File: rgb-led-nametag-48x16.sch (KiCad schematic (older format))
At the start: 21 parts, among them J1 USB_C_Receptacle_USB2.0, J2 TagConnect_TC2030_SWD, U25 STM32F722RETx, U26 SRV05-4, U27 TPS63001

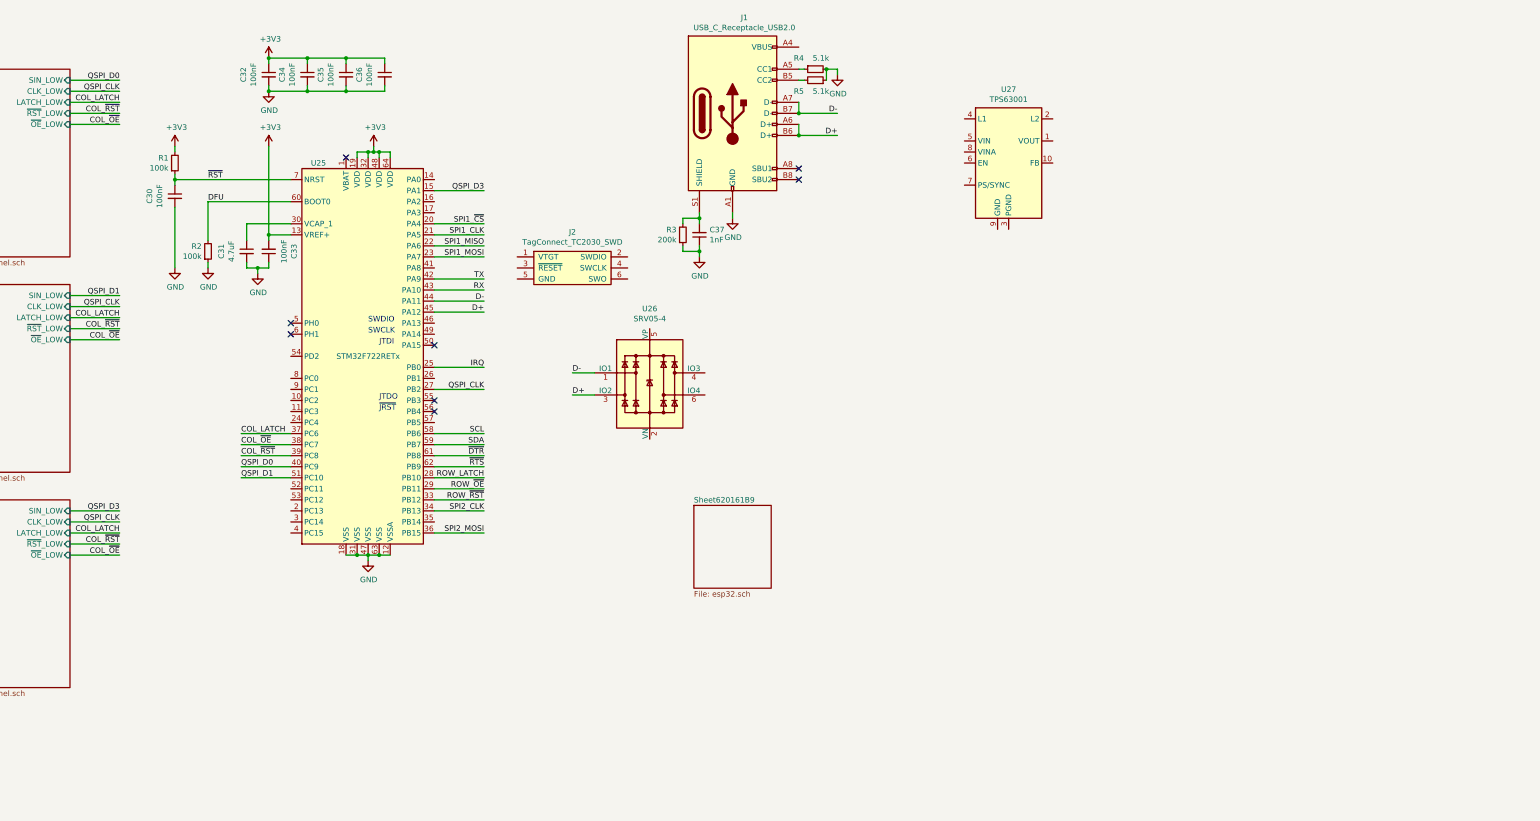
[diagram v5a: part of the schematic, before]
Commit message: Route ESP32 SPI bus
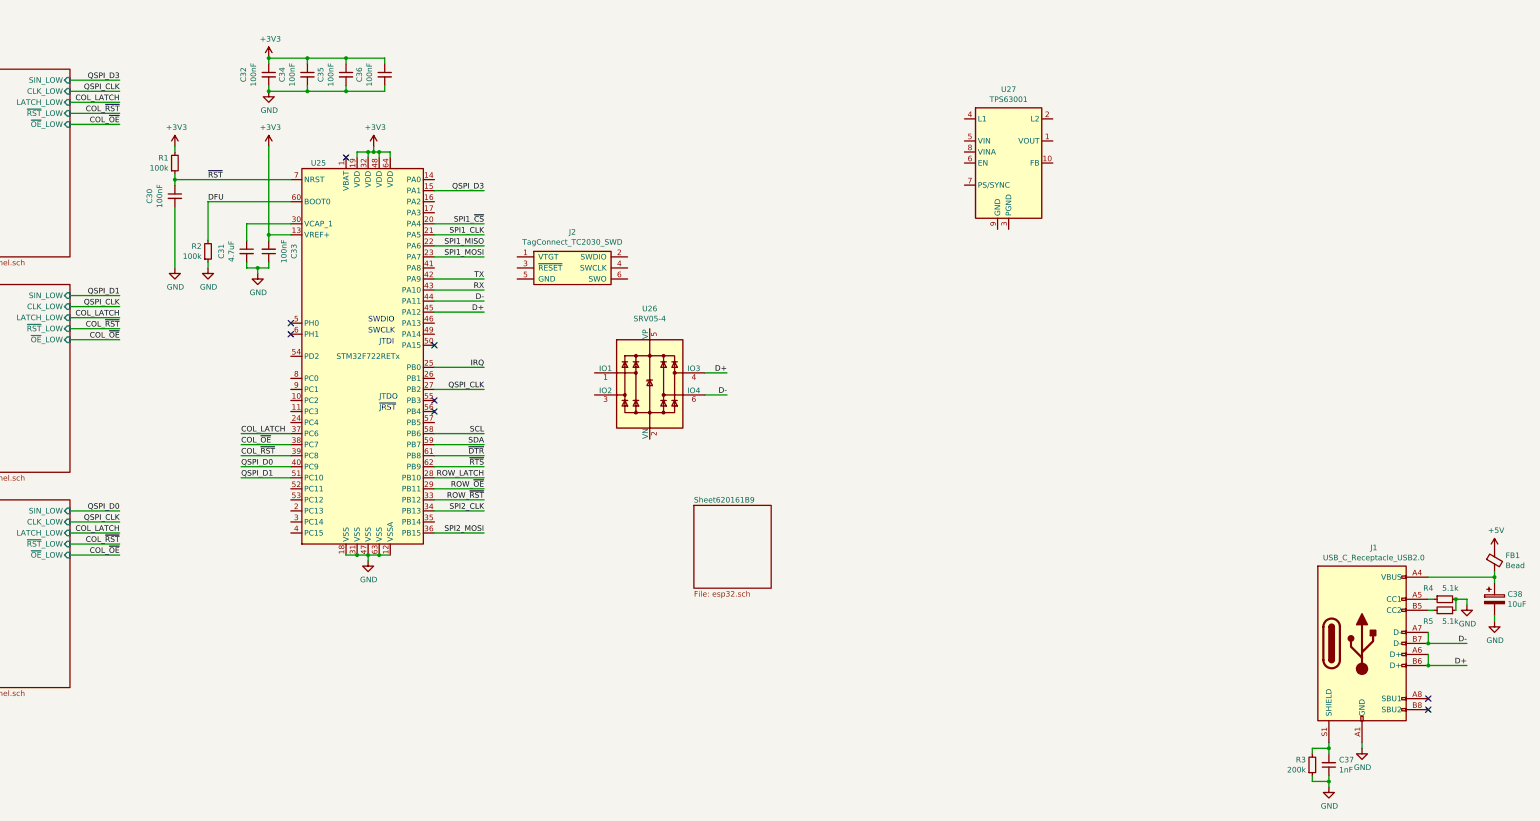
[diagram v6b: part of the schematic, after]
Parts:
- added C38: 10uF, Capacitor_Tantalum_SMD:CP_EIA-3216-10_Kemet-I, symbol Device:CP
- added FB1: Bead, Inductor_SMD:L_0805_2012Metric, symbol Device:Ferrite_Bead_Small
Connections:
- net D+: now also U26.4 (IO3); no longer U26.3 (IO2)
- net D-: now also U26.6 (IO4); no longer U26.1 (IO1)
- net GND: now also C38.2
- net at J1.A4 (VBUS), J1.A9 (VBUS), J1.B4 (VBUS)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: now also C38.1, FB1.2
- new net +5V: FB1.1
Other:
- moved on the sheet: C37, J1, R3, R4, R5

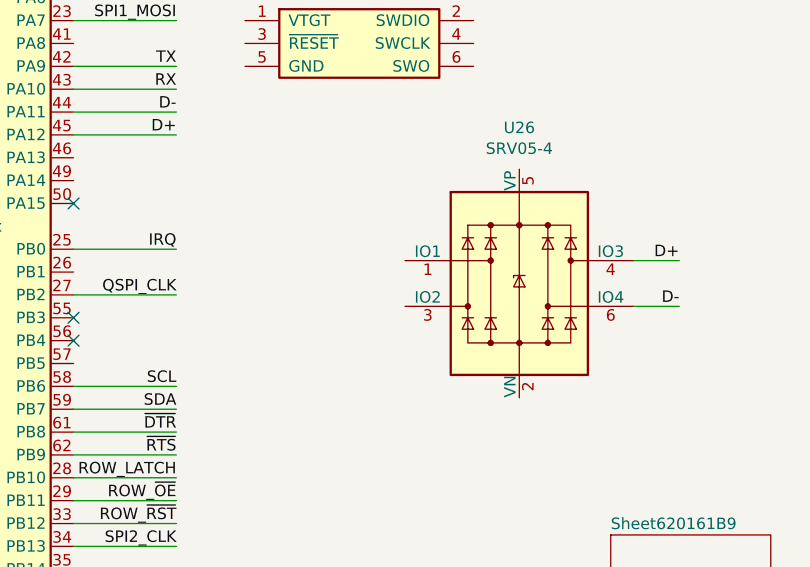
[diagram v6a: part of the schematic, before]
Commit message: Add preliminary ESP32 power layout
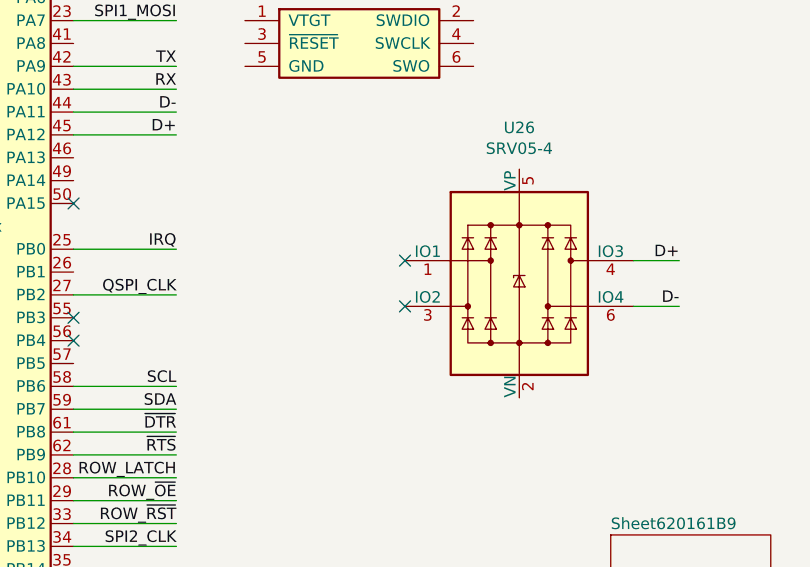
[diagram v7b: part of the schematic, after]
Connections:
- no-connect marks 9 -> 11
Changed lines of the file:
@@
 	1    0    0    -1
 $EndComp
+NoConn ~ 8850 3800
+NoConn ~ 8850 4000
 Wire Bus Line
 	2950 1250 2950 6650

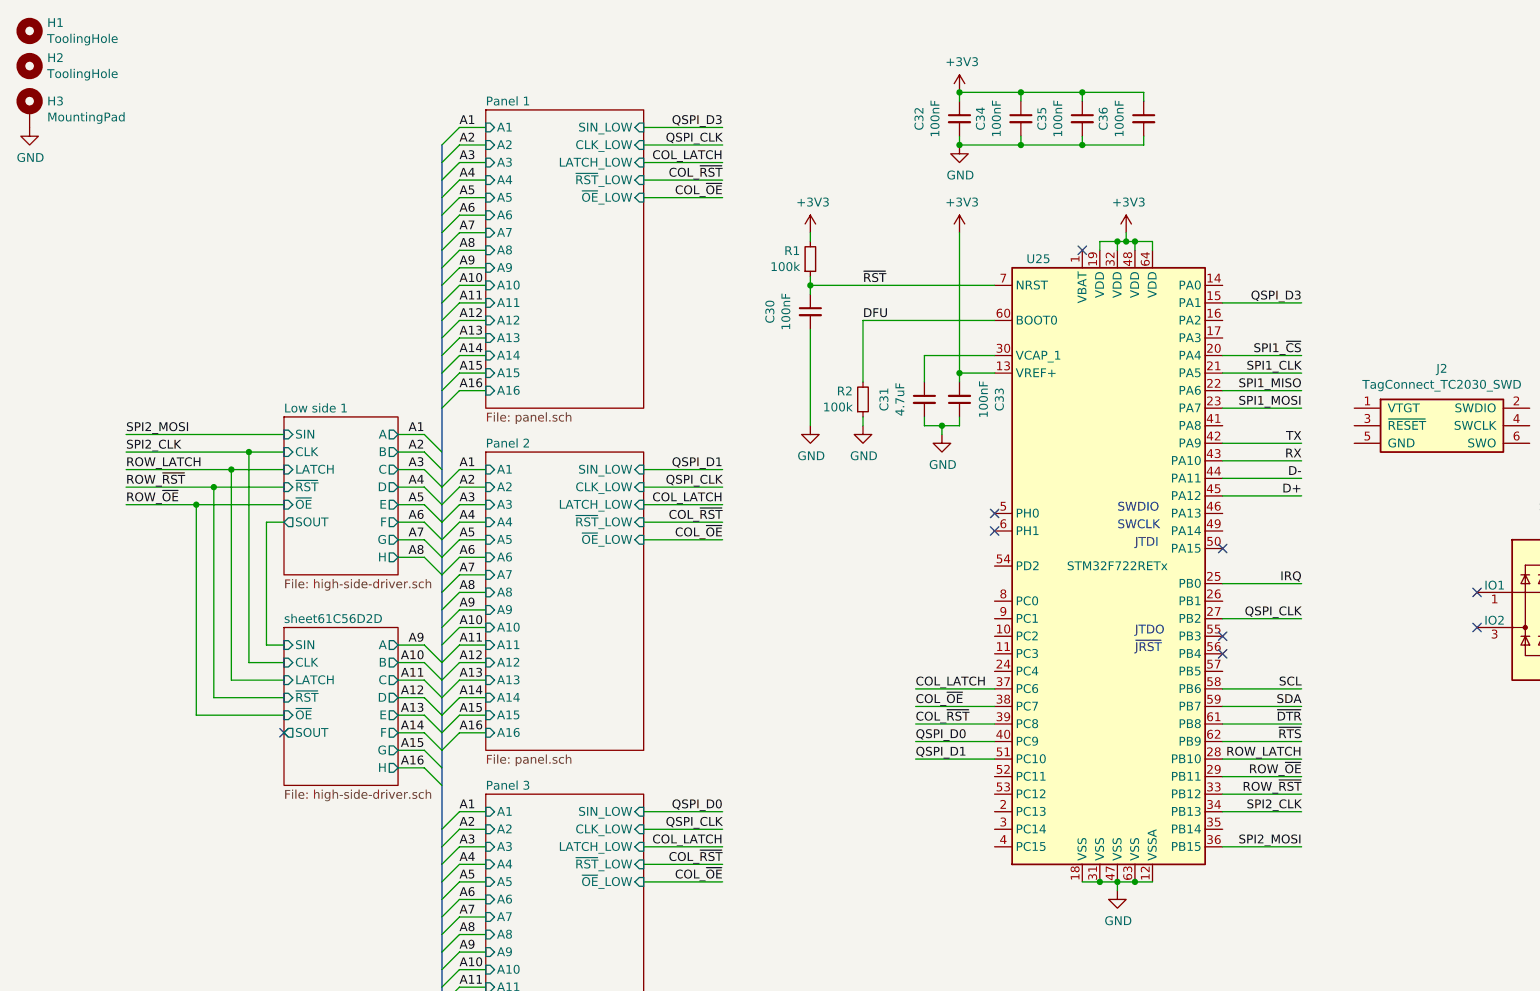
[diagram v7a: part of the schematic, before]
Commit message: Layout horizontal busses
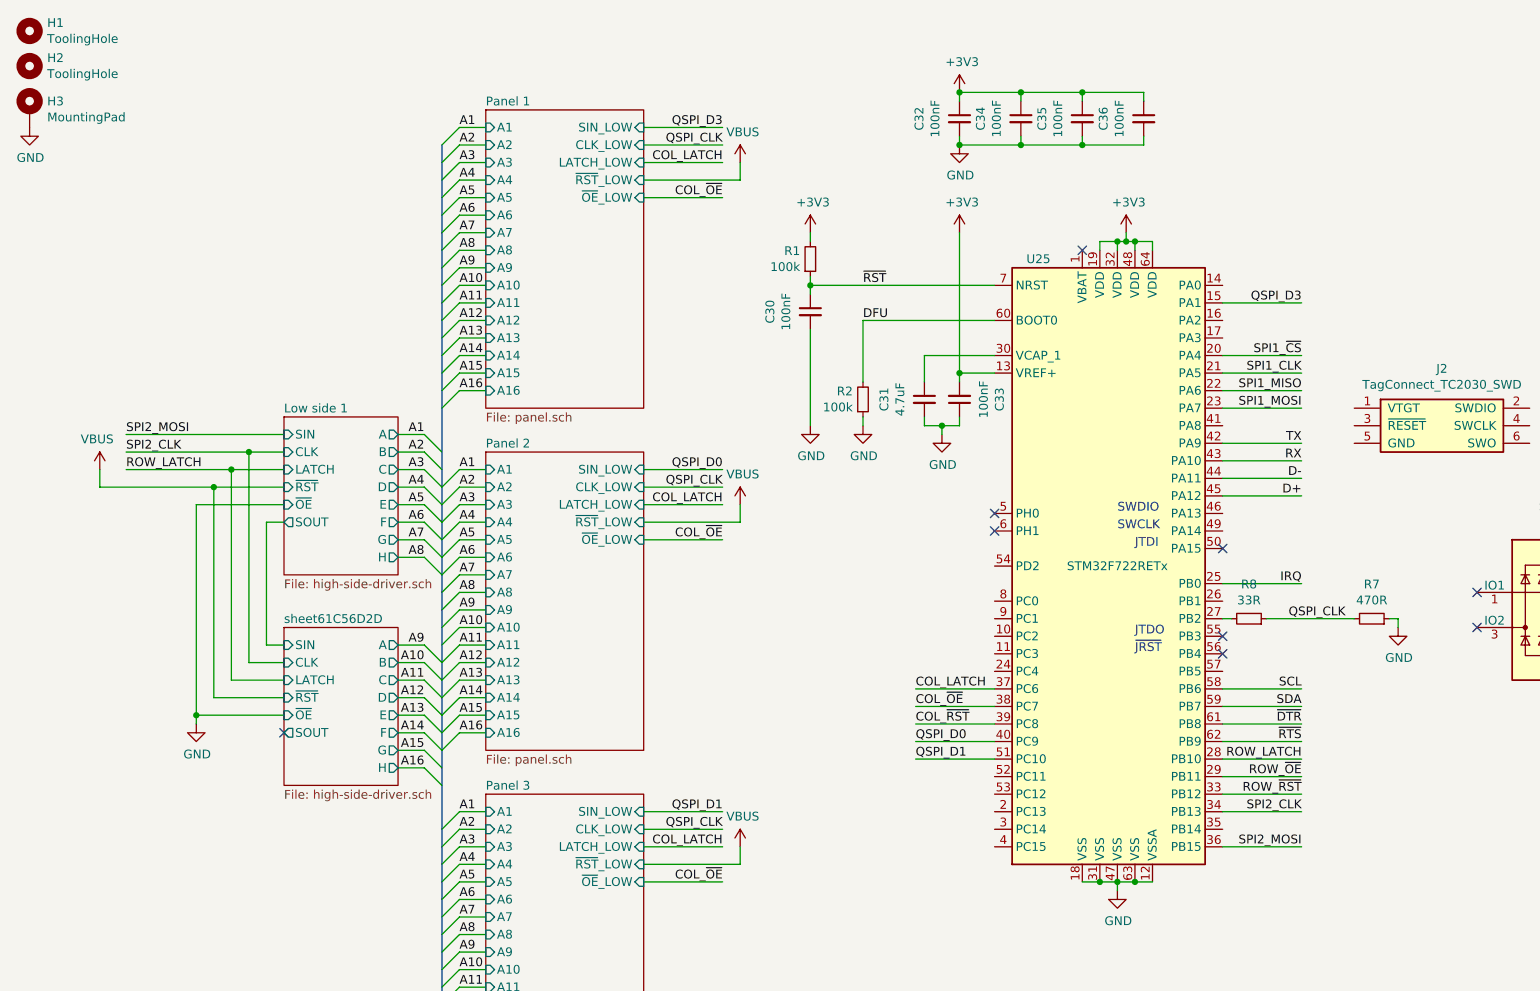
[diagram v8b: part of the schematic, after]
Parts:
- added R7: 470R, Resistor_SMD:R_0402_1005Metric, symbol Device:R_Small
- added R8: 33R, Resistor_SMD:R_0402_1005Metric, symbol Device:R_Small
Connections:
- net GND: now also R7.1
- net QSPI_CLK: now also R7.2, R8.1; no longer U25.27 (PB2)
- new net: R8.2, U25.27 (PB2)
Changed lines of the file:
@@
 Text Label 7850 2150 2    50   ~ 0
 QSPI_D3
-Text Label 7850 3950 2    50   ~ 0
-QSPI_CLK
 Text Label 5650 4650 0    50   ~ 0
 QSPI_D0
 Text Label 5650 4750 0    50   ~ 0
 QSPI_D1
-Text Label 4550 5050 2    50   ~ 0
+Text Label 4550 3100 2    50   ~ 0
 QSPI_D0
 Text Label 4550 1250 2    50   ~ 0
@@
 Connection ~ 1850 3000
 Wire Wire Line
-	1550 3300 1150 3300
-Connection ~ 1550 3300
-Text Label 1150 3300 0    50   ~ 0
-ROW_~OE
-Wire Wire Line
 	1750 3100 1150 3100
 Connection ~ 1750 3100
 Text Label 1150 3100 0    50   ~ 0
 ROW_LATCH
-Connection ~ 1650 3200
-Wire Wire Line
-	1150 3200 1650 3200
-Text Label 1150 3200 0    50   ~ 0
-ROW_~RST
 Text Label 4550 1350 2    50   ~ 0
 COL_LATCH
@@
 	4100 1350 4550 1350
 Wire Wire Line
-	4100 5050 4550 5050
+	4100 3100 4550 3100
 Wire Wire Line
 	4100 1250 4550 1250
 Wire Wire Line
-	4100 1450 4550 1450
-Text Label 4550 1450 2    50   ~ 0
-COL_~RST
-Wire Wire Line
 	4100 1550 4550 1550
-Text Label 4550 3100 2    50   ~ 0
+Text Label 4550 5050 2    50   ~ 0
 QSPI_D1
 Text Label 4550 3200 2    50   ~ 0
@@
 	4100 3300 4550 3300
 Wire Wire Line
-	4100 3100 4550 3100
+	4100 5050 4550 5050
 Wire Wire Line
 	4100 3200 4550 3200
-Wire Wire Line
-	4100 3400 4550 3400
-Text Label 4550 3400 2    50   ~ 0
-COL_~RST
 Wire Wire Line
 	4100 3500 4550 3500
@@
 	4100 5150 4550 5150
 Wire Wire Line
-	4100 5350 4550 5350
-Text Label 4550 5350 2    50   ~ 0
-COL_~RST
-Wire Wire Line
 	4100 5450 4550 5450
 Text Label 5650 4350 0    50   ~ 0
@@
 Wire Wire Line
 	7400 3250 7850 3250
-Wire Wire Line
-	7400 3950 7850 3950
 Wire Wire Line
 	5650 4650 6100 4650
@@
 NoConn ~ 8850 3800
 NoConn ~ 8850 4000
+$Comp
+L Device:R_Small R8
+U 1 1 622B250A
+P 7550 3950
+F 0 "R8" V 7746 3950 50  0000 C CNN
+F 1 "33R" V 7655 3950 50  0000 C CNN
+F 2 "Resistor_SMD:R_0402_1005Metric" H 7550 3950 50  0001 C CNN
+F 3 "~" H 7550 3950 50  0001 C CNN
+F 4 "C25105" H 7550 3950 50  0001 C CNN "LCSC"
+	1    7550 3950
+	0    1    -1   0
+$EndComp
+Wire Wire Line
+	7650 3950 8150 3950
+Wire Wire Line
+	8400 3950 8350 3950
+Wire Wire Line
+	8400 4000 8400 3950
+$Comp
+L power:GND #PWR0182
+U 1 1 62299123
+P 8400 4000
+F 0 "#PWR0182" H 8400 3750 50  0001 C CNN
+F 1 "GND" H 8405 3827 50  0000 C CNN
+F 2 "" H 8400 4000 50  0001 C CNN
+F 3 "" H 8400 4000 50  0001 C CNN
+	1    8400 4000
+	1    0    0    -1
+$EndComp
+$Comp
+L Device:R_Small R7
+U 1 1 6228DA41
+P 8250 3950
+F 0 "R7" V 8446 3950 50  0000 C CNN
+F 1 "470R" V 8355 3950 50  0000 C CNN
+F 2 "Resistor_SMD:R_0402_1005Metric" H 8250 3950 50  0001 C CNN
+F 3 "~" H 8250 3950 50  0001 C CNN
+F 4 "C25117" H 8250 3950 50  0001 C CNN "LCSC"
+	1    8250 3950
+	0    1    -1   0
+$EndComp
+Text Label 8100 3950 2    50   ~ 0
+QSPI_CLK
+Wire Wire Line
+	7450 3950 7400 3950
+$Comp
+L power:VBUS #PWR0183
+U 1 1 62303CE6
+P 4650 1350
+F 0 "#PWR0183" H 4650 1200 50  0001 C CNN
+F 1 "VBUS" H 4665 1523 50  0000 C CNN
+F 2 "" H 4650 1350 50  0001 C CNN
+F 3 "" H 4650 1350 50  0001 C CNN
+	1    4650 1350
+	1    0    0    -1
+$EndComp
+Wire Wire Line
+	4650 1350 4650 1450
+Wire Wire Line
+	4100 1450 4650 1450
+$Comp
+L power:VBUS #PWR0184
+U 1 1 6231C08B
+P 4650 3300
+F 0 "#PWR0184" H 4650 3150 50  0001 C CNN
+F 1 "VBUS" H 4665 3473 50  0000 C CNN
+F 2 "" H 4650 3300 50  0001 C CNN
+F 3 "" H 4650 3300 50  0001 C CNN
+	1    4650 3300
+	1    0    0    -1
+$EndComp
+Wire Wire Line
+	4650 3300 4650 3400
+Wire Wire Line
+	4100 3400 4650 3400
+$Comp
+L power:VBUS #PWR0185
+U 1 1 62333C4A
+P 4650 5250
+F 0 "#PWR0185" H 4650 5100 50  0001 C CNN
+F 1 "VBUS" H 4665 5423 50  0000 C CNN
+F 2 "" H 4650 5250 50  0001 C CNN
+F 3 "" H 4650 5250 50  0001 C CNN
+	1    4650 5250
+	1    0    0    -1
+$EndComp
+Wire Wire Line
+	4650 5250 4650 5350
+Wire Wire Line
+	4100 5350 4650 5350
+$Comp
+L power:VBUS #PWR0186
+U 1 1 6234B95B
+P 1000 3100
+F 0 "#PWR0186" H 1000 2950 50  0001 C CNN
+F 1 "VBUS" H 1015 3273 50  0000 C CNN
+F 2 "" H 1000 3100 50  0001 C CNN
+F 3 "" H 1000 3100 50  0001 C CNN
+	1    1000 3100
+	-1   0    0    -1
+$EndComp
+Wire Wire Line
+	1000 3100 1000 3200
+Wire Wire Line
+	1000 3200 1650 3200
+Connection ~ 1650 3200
+$Comp
+L power:GND #PWR0187
+U 1 1 6236520D
+P 1550 4550
+F 0 "#PWR0187" H 1550 4300 50  0001 C CNN
+F 1 "GND" H 1555 4377 50  0000 C CNN
+F 2 "" H 1550 4550 50  0001 C CNN
+F 3 "" H 1550 4550 50  0001 C CNN
+	1    1550 4550
+	1    0    0    -1
+$EndComp
+Wire Wire Line
+	1550 4550 1550 4500
+Connection ~ 1550 4500
 Wire Bus Line
 	2950 1250 2950 6650
